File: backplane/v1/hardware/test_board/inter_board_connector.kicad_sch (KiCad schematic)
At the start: 1 part, among them J1 Conn_02x20_Odd_Even

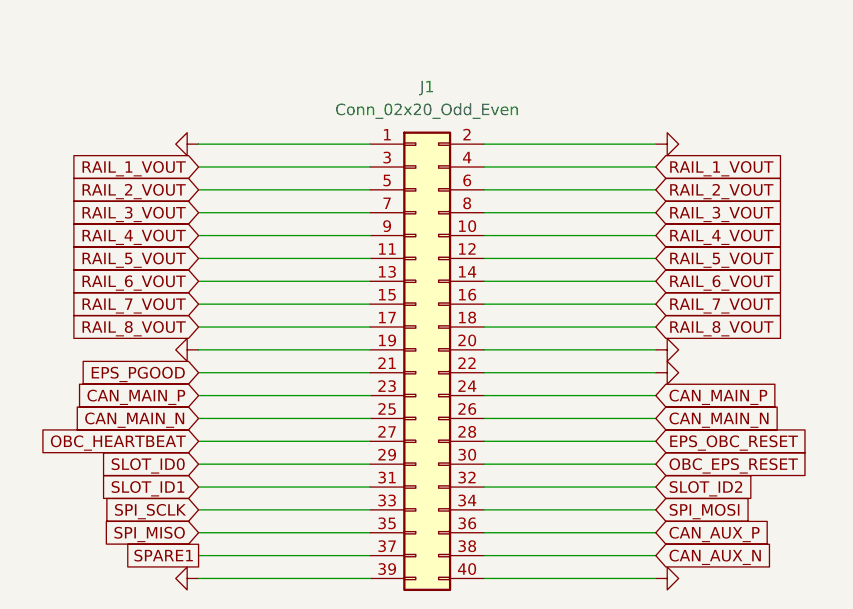
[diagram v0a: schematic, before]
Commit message: add zone keepouts
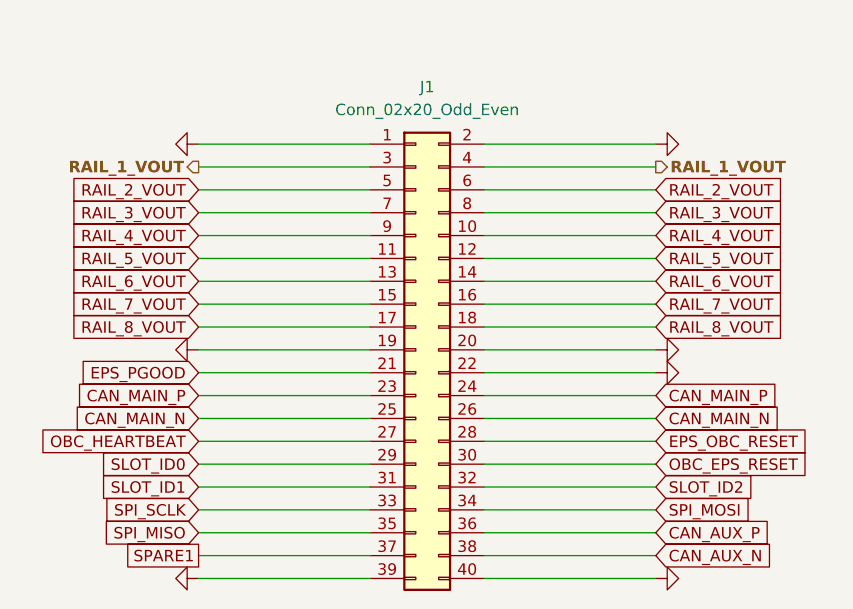
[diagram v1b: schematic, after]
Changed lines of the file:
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@@
-		)
-	)
-	(global_label "RAIL_1_VOUT"
-		(shape input)
-		(at 101.6 72.39 180)
-		(fields_autoplaced yes)
-		(effects
-			(font
-				(size 1.27 1.27)
-			)
-			(justify right)
-		)
-		(property "Intersheetrefs" "${INTERSHEET_REFS}"
-			(at 86.7614 72.39 0)
-			(hide yes)
-			(show_name no)
-			(do_not_autoplace no)
-			(effects
-				(font
-					(size 1.27 1.27)
-				)
-				(justify right)
-			)
 		)
 	)
@@
 		)
 	)
-	(global_label "RAIL_1_VOUT"
-		(shape input)
-		(at 152.4 72.39 0)
-		(fields_autoplaced yes)
+	(hierarchical_label "RAIL_1_VOUT"
+		(shape output)
+		(at 101.6 72.39 180)
 		(effects
 			(font
 				(size 1.27 1.27)
+				(thickness 0.254)
+				(bold yes)
+			)
+			(justify right)
+		)
+	)
+	(hierarchical_label "RAIL_1_VOUT"
+		(shape output)
+		(at 152.4 72.39 0)
+		(effects
+			(font
+				(size 1.27 1.27)
+				(thickness 0.254)
+				(bold yes)
 			)
 			(justify left)
 		)
-		(property "Intersheetrefs" "${INTERSHEET_REFS}"
-			(at 167.2386 72.39 0)
-			(hide yes)
-			(show_name no)
-			(do_not_autoplace no)
-			(effects
-				(font
-					(size 1.27 1.27)
-				)
-				(justify left)
-			)
-		)
 	)

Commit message: add burnwire & IMU peripherals
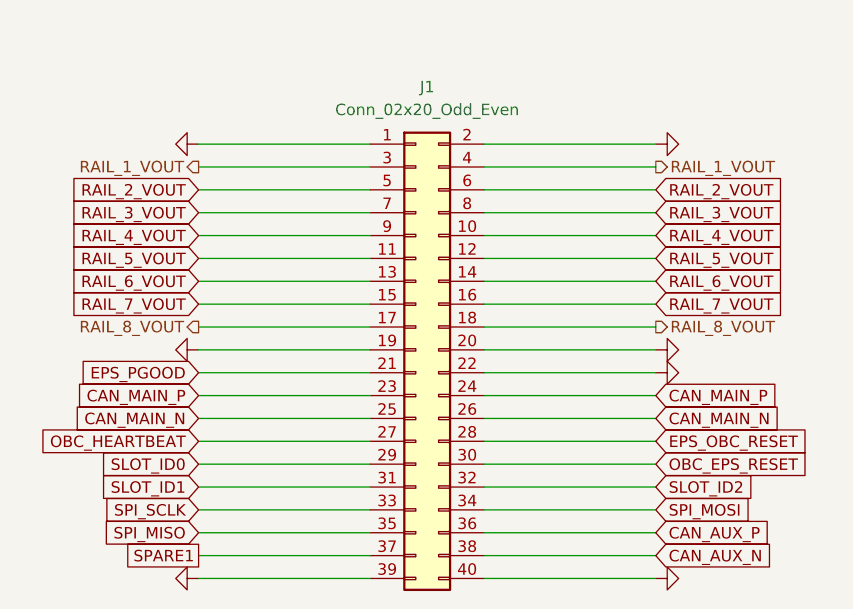
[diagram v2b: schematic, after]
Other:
- title: (none) -> Daughterboard
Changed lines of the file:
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@@
 	(generator_version "10.0")
 	(paper "A4")
+	(title_block
+		(title "Daughterboard")
+	)
 	(wire
 		(pts
@@
 		)
 	)
-	(global_label "RAIL_8_VOUT"
-		(shape input)
-		(at 152.4 90.17 0)
-		(fields_autoplaced yes)
-		(effects
-			(font
-				(size 1.27 1.27)
-			)
-			(justify left)
-		)
-		(property "Intersheetrefs" "${INTERSHEET_REFS}"
-			(at 167.2386 90.17 0)
-			(hide yes)
-			(show_name no)
-			(do_not_autoplace no)
-			(effects
-				(font
-					(size 1.27 1.27)
-				)
-				(justify left)
-			)
-		)
-	)
 	(global_label "RAIL_2_VOUT"
 		(shape input)
@@
 		(property "Intersheetrefs" "${INTERSHEET_REFS}"
 			(at 86.7614 77.47 0)
-			(hide yes)
-			(show_name no)
-			(do_not_autoplace no)
-			(effects
-				(font
-					(size 1.27 1.27)
-				)
-				(justify right)
-			)
-		)
-	)
-	(global_label "RAIL_8_VOUT"
-		(shape input)
-		(at 101.6 90.17 180)
-		(fields_autoplaced yes)
-		(effects
-			(font
-				(size 1.27 1.27)
-			)
-			(justify right)
-		)
-		(property "Intersheetrefs" "${INTERSHEET_REFS}"
-			(at 86.7614 90.17 0)
 			(hide yes)
 			(show_name no)
@@
 			(font
 				(size 1.27 1.27)
-				(thickness 0.254)
-				(bold yes)
-			)
-			(justify right)
+				(thickness 0.1588)
+			)
+			(justify right)
+		)
+	)
+	(hierarchical_label "RAIL_8_VOUT"
+		(shape output)
+		(at 101.6 90.17 180)
+		(effects
+			(font
+				(size 1.27 1.27)
+				(thickness 0.1588)
+			)
+			(justify right)
+		)
+	)
+	(hierarchical_label "RAIL_8_VOUT"
+		(shape output)
+		(at 152.4 90.17 0)
+		(effects
+			(font
+				(size 1.27 1.27)
+				(thickness 0.1588)
+			)
+			(justify left)
 		)
 	)
@@
 			(font
 				(size 1.27 1.27)
-				(thickness 0.254)
-				(bold yes)
-			)
-			(justify left)
+				(thickness 0.1588)
+			)
+			(justify left)

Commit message: add ADC peripherals to test board
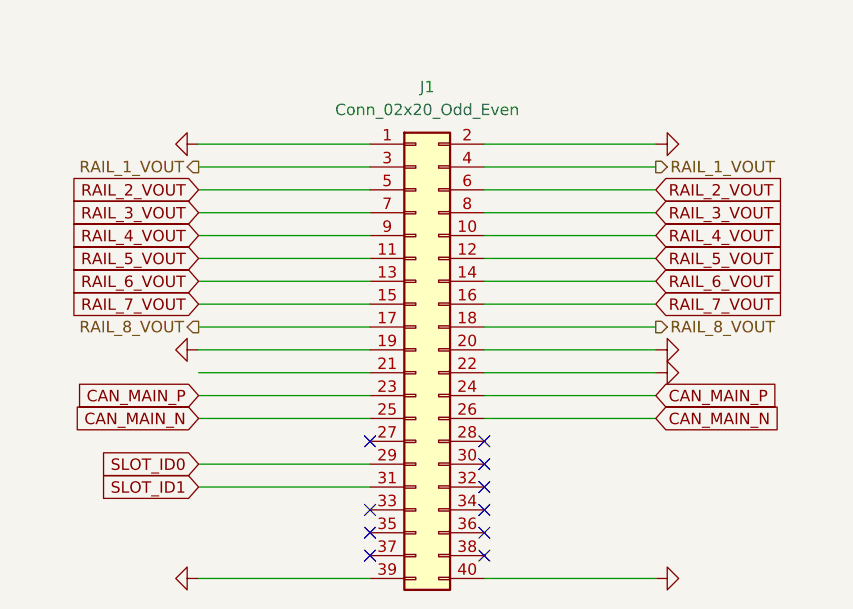
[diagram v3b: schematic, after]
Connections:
- net CAN_AUX_N: no longer names the net of J1.38 (Pin_38)
- net CAN_AUX_P: no longer names the net of J1.36 (Pin_36)
- net EPS_OBC_RESET: no longer names the net of J1.28 (Pin_28)
- net EPS_PGOOD: no longer names the net of J1.21 (Pin_21)
- net OBC_EPS_RESET: no longer names the net of J1.30 (Pin_30)
- net OBC_HEARTBEAT: no longer names the net of J1.27 (Pin_27)
- net SLOT_ID2: no longer names the net of J1.32 (Pin_32)
- net SPARE1: no longer names the net of J1.37 (Pin_37)
- net SPI_MISO: no longer names the net of J1.35 (Pin_35)
- net SPI_MOSI: no longer names the net of J1.34 (Pin_34)
- net SPI_SCLK: no longer names the net of J1.33 (Pin_33)
- no-connect marks 0 -> 10

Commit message: continue adding peripherals
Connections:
- no-connect marks 10 -> 11
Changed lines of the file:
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@@
+	)
+	(no_connect
+		(at 120.65 95.25)
 	)
 	(no_connect
@@
 		)
 		(stroke
-			(width 0)
-			(type default)
-		)
-	)
-	(wire
-		(pts
-			(xy 101.6 95.25) (xy 120.65 95.25)
-		)
-		(stroke

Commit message: finalize schematic
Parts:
- J1: footprint footprints:J-SAMTEC-TFM-120-X1-XXX-D-RA -> OSUSAT_Connectors:J-SAMTEC-TFM-120-X1-XXX-D-RA
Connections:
- net SLOT_ID0: no longer names the net of J1.29 (Pin_29)
- net SLOT_ID1: no longer names the net of J1.31 (Pin_31)
- no-connect marks 11 -> 13
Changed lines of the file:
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@@
 		(title "Daughterboard")
+	)
+	(junction
+		(at 110.49 69.85)
+		(diameter 0)
+		(color 0 0 0 0)
 	)
 	(no_connect
@@
 	)
 	(no_connect
+		(at 120.65 105.41)
+	)
+	(no_connect
 		(at 133.35 102.87)
 	)
@@
 	)
 	(no_connect
+		(at 120.65 107.95)
+	)
+	(no_connect
 		(at 133.35 110.49)
 	)
@@
 	(wire
 		(pts
+			(xy 110.49 62.23) (xy 110.49 69.85)
+		)
+		(stroke
+			(width 0)
+			(type default)
+		)
+	)
+	(wire
+		(pts
 			(xy 133.35 69.85) (xy 152.4 69.85)
 		)
@@
 	(wire
 		(pts
-			(xy 101.6 69.85) (xy 120.65 69.85)
+			(xy 101.6 69.85) (xy 110.49 69.85)
 		)
 		(stroke
@@
 	(wire
 		(pts
+			(xy 110.49 69.85) (xy 120.65 69.85)
+		)
+		(stroke
+			(width 0)
+			(type default)
+		)
+	)
+	(wire
+		(pts
 			(xy 133.35 100.33) (xy 152.4 100.33)
 		)
@@
 	(wire
 		(pts
-			(xy 101.6 107.95) (xy 120.65 107.95)
-		)
-		(stroke
-			(width 0)
-			(type default)
-		)
-	)
-	(wire
-		(pts
-			(xy 101.6 105.41) (xy 120.65 105.41)
-		)
-		(stroke
-			(width 0)
-			(type default)
-		)
-	)
-	(wire
-		(pts
 			(xy 133.35 72.39) (xy 152.4 72.39)
 		)
@@
 		)
 	)
-	(global_label "SLOT_ID1"
-		(shape input)
-		(at 101.6 107.95 180)
+	(global_label "RAIL_4_VOUT"
+		(shape input)
+		(at 152.4 80.01 0)
+		(fields_autoplaced yes)
+		(effects
+			(font
+				(size 1.27 1.27)
+			)
+			(justify left)
+		)
+		(property "Intersheetrefs" "${INTERSHEET_REFS}"
+			(at 167.2386 80.01 0)
+			(hide yes)
+			(show_name no)
+			(do_not_autoplace no)
+			(effects
+				(font
+					(size 1.27 1.27)
+				)
+				(justify left)
+			)
+		)
+	)
+	(global_label "RAIL_6_VOUT"
+		(shape input)
+		(at 152.4 85.09 0)
+		(fields_autoplaced yes)
+		(effects
+			(font
+				(size 1.27 1.27)
+			)
+			(justify left)
+		)
+		(property "Intersheetrefs" "${INTERSHEET_REFS}"
+			(at 167.2386 85.09 0)
+			(hide yes)
+			(show_name no)
+			(do_not_autoplace no)
+			(effects
+				(font
+					(size 1.27 1.27)
+				)
+				(justify left)
+			)
+		)
+	)
+	(global_label "CAN_MAIN_N"
+		(shape input)
+		(at 101.6 100.33 180)
 		(fields_autoplaced yes)
 		(effects
@@
 		)
 		(property "Intersheetrefs" "${INTERSHEET_REFS}"
-			(at 90.0272 107.95 0)
+			(at 87.1847 100.33 0)
 			(hide yes)
 			(show_name no)
@@
 		)
 	)
-	(global_label "RAIL_4_VOUT"
-		(shape input)
-		(at 152.4 80.01 0)
-		(fields_autoplaced yes)
-		(effects
-			(font
-				(size 1.27 1.27)
-			)
-			(justify left)
-		)
-		(property "Intersheetrefs" "${INTERSHEET_REFS}"
-			(at 167.2386 80.01 0)
-			(hide yes)
-			(show_name no)
-			(do_not_autoplace no)
-			(effects
-				(font
-					(size 1.27 1.27)
-				)
-				(justify left)
-			)
-		)
-	)
-	(global_label "RAIL_6_VOUT"
-		(shape input)
-		(at 152.4 85.09 0)
-		(fields_autoplaced yes)
-		(effects
-			(font
-				(size 1.27 1.27)
-			)
-			(justify left)
-		)
-		(property "Intersheetrefs" "${INTERSHEET_REFS}"
-			(at 167.2386 85.09 0)
-			(hide yes)
-			(show_name no)
-			(do_not_autoplace no)
-			(effects
-				(font
-					(size 1.27 1.27)
-				)
-				(justify left)
-			)
-		)
-	)
-	(global_label "CAN_MAIN_N"
-		(shape input)
-		(at 101.6 100.33 180)
+	(global_label "RAIL_2_VOUT"
+		(shape input)
+		(at 101.6 74.93 180)
 		(fields_autoplaced yes)
 		(effects
@@
 		)
 		(property "Intersheetrefs" "${INTERSHEET_REFS}"
-			(at 87.1847 100.33 0)
-			(hide yes)
-			(show_name no)
-			(do_not_autoplace no)
-			(effects
-				(font
-					(size 1.27 1.27)
-				)
-				(justify right)
-			)
-		)
-	)
-	(global_label "RAIL_2_VOUT"
-		(shape input)
-		(at 101.6 74.93 180)
-		(fields_autoplaced yes)
-		(effects
-			(font
-				(size 1.27 1.27)
-			)
-			(justify right)
-		)
-		(property "Intersheetrefs" "${INTERSHEET_REFS}"
 			(at 86.7614 74.93 0)
-			(hide yes)
-			(show_name no)
-			(do_not_autoplace no)
-			(effects
-				(font
-					(size 1.27 1.27)
-				)
-				(justify right)
-			)
-		)
-	)
-	(global_label "SLOT_ID0"
-		(shape input)
-		(at 101.6 105.41 180)
-		(fields_autoplaced yes)
-		(effects
-			(font
-				(size 1.27 1.27)
-			)
-			(justify right)
-		)
-		(property "Intersheetrefs" "${INTERSHEET_REFS}"
-			(at 90.0272 105.41 0)
 			(hide yes)
 			(show_name no)
@@
 	)
 	(symbol
+		(lib_id "power:PWR_FLAG")
+		(at 110.49 62.23 0)
+		(unit 1)
+		(body_style 1)
+		(exclude_from_sim no)
+		(in_bom yes)
+		(on_board yes)
+		(in_pos_files yes)
+		(dnp no)
+		(fields_autoplaced yes)
+		(property "Reference" "#FLG04"
+			(at 110.49 60.325 0)
+			(hide yes)
+			(show_name no)
+			(do_not_autoplace no)
+			(effects
+				(font
+					(size 1.27 1.27)
+				)
+			)
+		)
+		(property "Value" "PWR_FLAG"
+			(at 110.49 57.15 0)
+			(show_name no)
+			(do_not_autoplace no)
+			(effects
+				(font
+					(size 1.27 1.27)
+				)
+			)
+		)
+		(property "Footprint" ""
+			(at 110.49 62.23 0)
+			(hide yes)
+			(show_name no)
+			(do_not_autoplace no)
+			(effects
+				(font
+					(size 1.27 1.27)
+				)
+			)
+		)
+		(property "Datasheet" ""
+			(at 110.49 62.23 0)
+			(hide yes)
+			(show_name no)
+			(do_not_autoplace no)
+			(effects
+				(font
+					(size 1.27 1.27)
+				)
+			)
+		)
+		(property "Description" "Special symbol for telling ERC where power comes from"
+			(at 110.49 62.23 0)
+			(hide yes)
+			(show_name no)
+			(do_not_autoplace no)
+			(effects
+				(font
+					(size 1.27 1.27)
+				)
+			)
+		)
+		(pin "1"
+		)
+		(instances
+			(project "test_board"
+				(path "/b20f5a9e-495e-48d8-8648-bd5c7d9b4620/d7776c9d-110d-4867-b7e7-ee23b34eac43"
+					(reference "#FLG04")
+					(unit 1)
+				)
+			)
+		)
+	)
+	(symbol
 		(lib_id "power:GND")
 		(at 101.6 118.11 270)
@@
 			)
 		)
-		(property "Footprint" "footprints:J-SAMTEC-TFM-120-X1-XXX-D-RA"
+		(property "Footprint" "OSUSAT_Connectors:J-SAMTEC-TFM-120-X1-XXX-D-RA"
 			(at 125.73 92.71 0)
 			(hide yes)

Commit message: start layout
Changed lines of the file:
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@@
-		)
-	)
-	(global_label "CAN_MAIN_N"
-		(shape input)
-		(at 152.4 100.33 0)
-		(fields_autoplaced yes)
-		(effects
-			(font
-				(size 1.27 1.27)
-			)
-			(justify left)
-		)
-		(property "Intersheetrefs" "${INTERSHEET_REFS}"
-			(at 166.5129 100.33 0)
-			(hide yes)
-			(show_name no)
-			(do_not_autoplace no)
-			(effects
-				(font
-					(size 1.27 1.27)
-				)
-				(justify left)
-			)
 		)
 	)
@@
 		)
 	)
-	(global_label "CAN_MAIN_P"
-		(shape input)
-		(at 152.4 97.79 0)
-		(fields_autoplaced yes)
-		(effects
-			(font
-				(size 1.27 1.27)
-			)
-			(justify left)
-		)
-		(property "Intersheetrefs" "${INTERSHEET_REFS}"
-			(at 166.8153 97.79 0)
-			(hide yes)
-			(show_name no)
-			(do_not_autoplace no)
-			(effects
-				(font
-					(size 1.27 1.27)
-				)
-				(justify left)
-			)
-		)
-	)
 	(global_label "RAIL_7_VOUT"
 		(shape input)
@@
 		)
 	)
-	(global_label "CAN_MAIN_N"
-		(shape input)
-		(at 101.6 100.33 180)
-		(fields_autoplaced yes)
-		(effects
-			(font
-				(size 1.27 1.27)
-			)
-			(justify right)
-		)
-		(property "Intersheetrefs" "${INTERSHEET_REFS}"
-			(at 87.1847 100.33 0)
-			(hide yes)
-			(show_name no)
-			(do_not_autoplace no)
-			(effects
-				(font
-					(size 1.27 1.27)
-				)
-				(justify right)
-			)
-		)
-	)
 	(global_label "RAIL_2_VOUT"
 		(shape input)
@@
 		(property "Intersheetrefs" "${INTERSHEET_REFS}"
 			(at 86.7614 74.93 0)
-			(hide yes)
-			(show_name no)
-			(do_not_autoplace no)
-			(effects
-				(font
-					(size 1.27 1.27)
-				)
-				(justify right)
-			)
-		)
-	)
-	(global_label "CAN_MAIN_P"
-		(shape input)
-		(at 101.6 97.79 180)
-		(fields_autoplaced yes)
-		(effects
-			(font
-				(size 1.27 1.27)
-			)
-			(justify right)
-		)
-		(property "Intersheetrefs" "${INTERSHEET_REFS}"
-			(at 87.2452 97.79 0)
 			(hide yes)
 			(show_name no)
@@
 		)
 	)
+	(hierarchical_label "CAN_MAIN_N"
+		(shape bidirectional)
+		(at 152.4 100.33 0)
+		(effects
+			(font
+				(size 1.27 1.27)
+			)
+			(justify left)
+		)
+	)
 	(hierarchical_label "RAIL_1_VOUT"
 		(shape output)
@@
 			)
 			(justify left)
+		)
+	)
+	(hierarchical_label "CAN_MAIN_P"
+		(shape bidirectional)
+		(at 101.6 97.79 180)
+		(effects
+			(font
+				(size 1.27 1.27)
+			)
+			(justify right)
+		)
+	)
+	(hierarchical_label "CAN_MAIN_N"
+		(shape bidirectional)
+		(at 101.6 100.33 180)
+		(effects
+			(font
+				(size 1.27 1.27)
+			)
+			(justify right)
+		)
+	)
+	(hierarchical_label "CAN_MAIN_P"
+		(shape bidirectional)
+		(at 152.4 97.79 0)
+		(effects
+			(font
+				(size 1.27 1.27)
+			)
+			(justify left)
